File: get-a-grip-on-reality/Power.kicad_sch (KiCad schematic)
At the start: 40 parts, among them J14 Conn_01x05_Pin, J15 Battery Connector Bat, U6 BQ25887, U7 TPS54KB20RZRR

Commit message: finish pcb no drc errors
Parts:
- U7: footprint fydp library:RZR0016A-MFG -> fydp:RZR0016A-MFG
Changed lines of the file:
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@@
 			)
 		)
-		(property "Footprint" "fydp library:RZR0016A-MFG"
+		(property "Footprint" "fydp:RZR0016A-MFG"
 			(at 129.54 43.18 0)
 			(effects

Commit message: fixes to pcb
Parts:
- added P2: USB_C_Plug_USB2.0, Connector_USB:USB_C_Receptacle_GCT_USB4110, symbol Connector:USB_C_Plug_USB2.0
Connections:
- net GND: now also P2.A1 (GND), P2.A12 (GND), P2.B1 (GND), P2.B12 (GND), P2.S1 (SHIELD); no longer D7.2 (A)
- net +5V renamed +5VBuck
- net +5VBuck: no longer C14.1, D8.2 (A2), U6.23 (VBUS)
- new net: P2.A6 (D+), P2.A7 (D-)
- new net +5VUSB: C14.1, D7.2 (A), D8.2 (A2), P2.A4 (VBUS), P2.A9 (VBUS), P2.B4 (VBUS), P2.B9 (VBUS), U6.23 (VBUS)
- no-connect marks 2 -> 4
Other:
- moved on the sheet: BT1, C14, C21, C24, C25, C26, D7, D8, J14, J15, L1, R12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

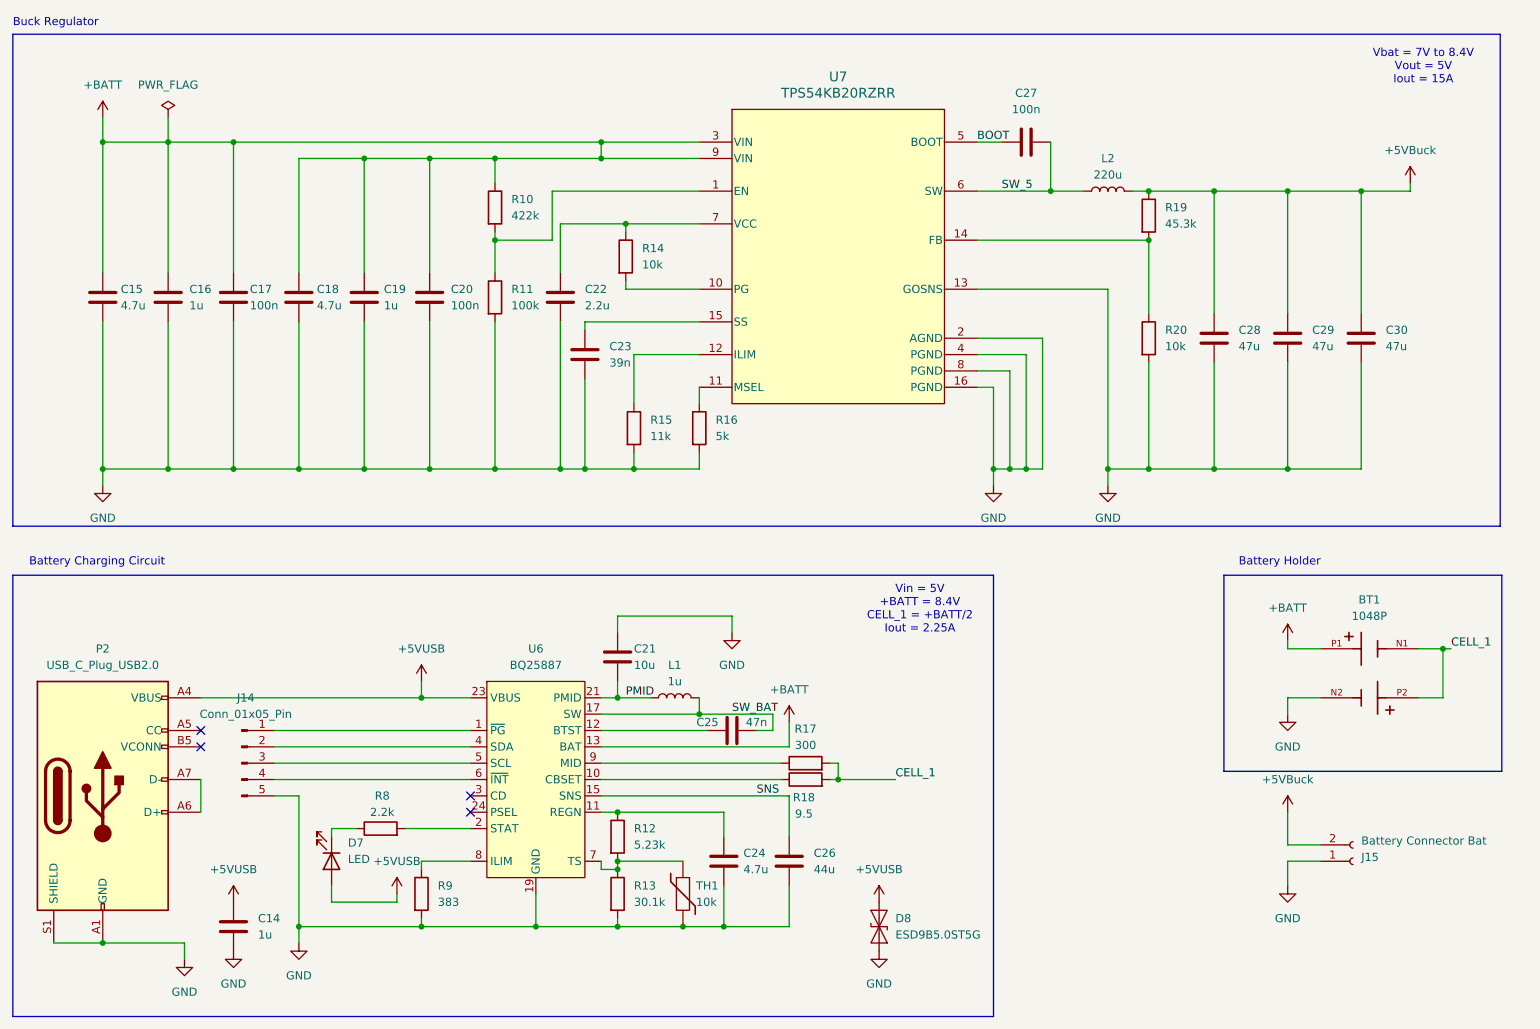
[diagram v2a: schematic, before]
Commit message: add mobile demo and rtos version of glove, improve schematic
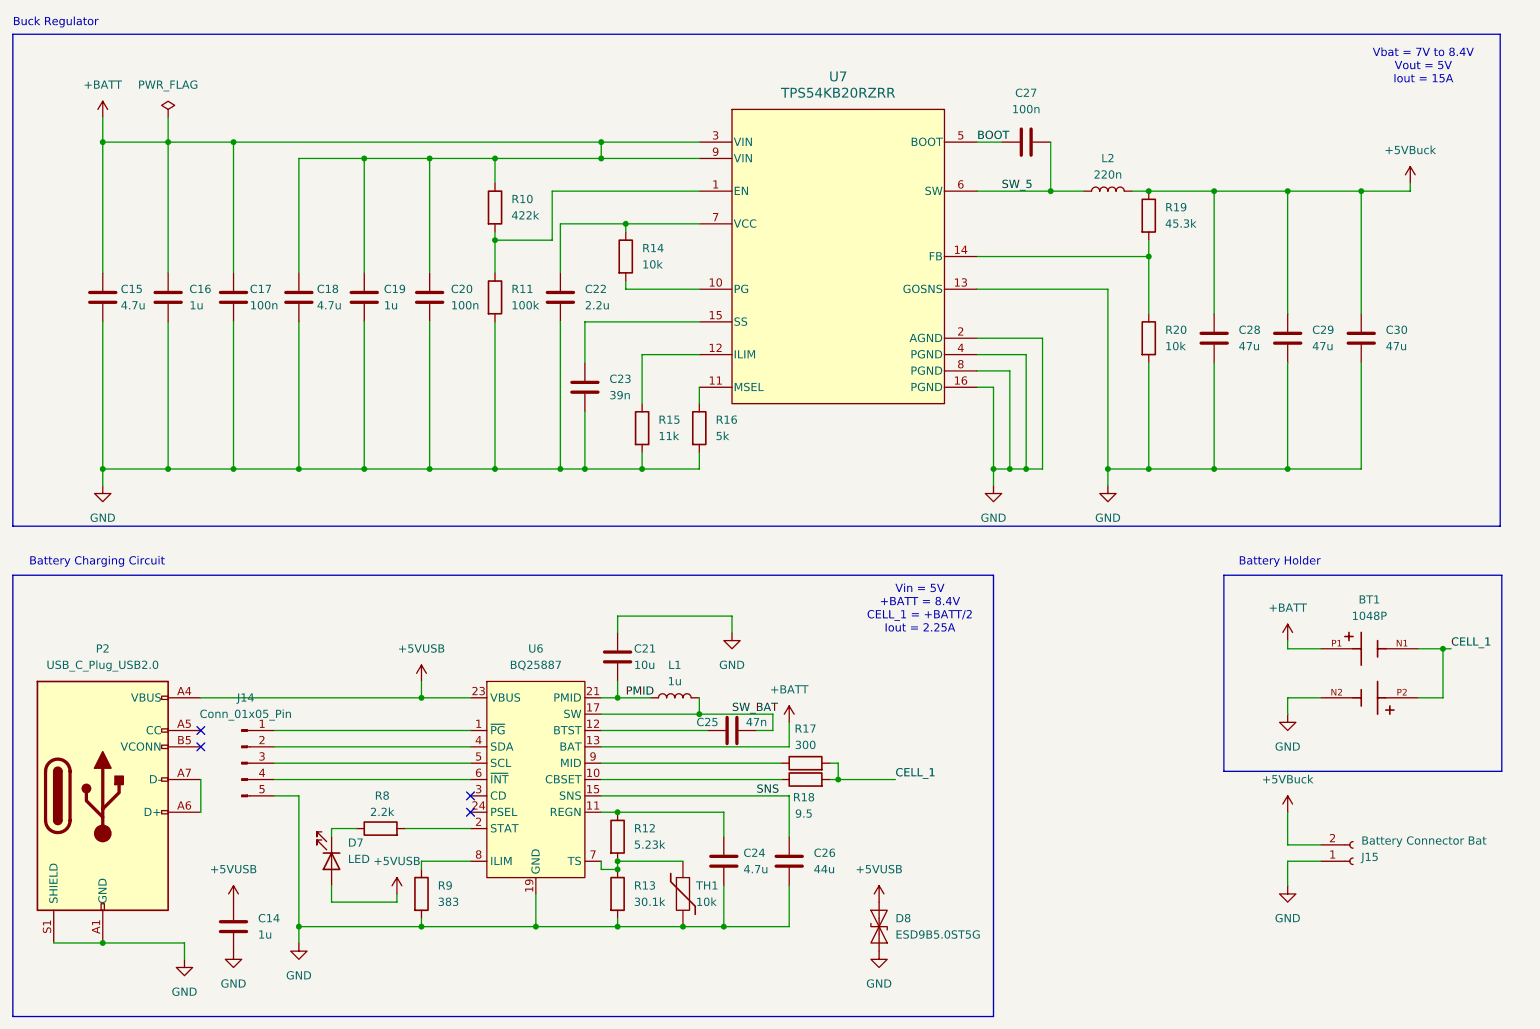
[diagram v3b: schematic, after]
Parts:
- L2: value 220u -> 220n
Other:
- moved on the sheet: C23, R15
